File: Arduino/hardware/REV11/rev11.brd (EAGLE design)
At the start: 71 x 53 mm, 30 parts, among them IC2 ATMEGA168-AU, Q1 32768Hz

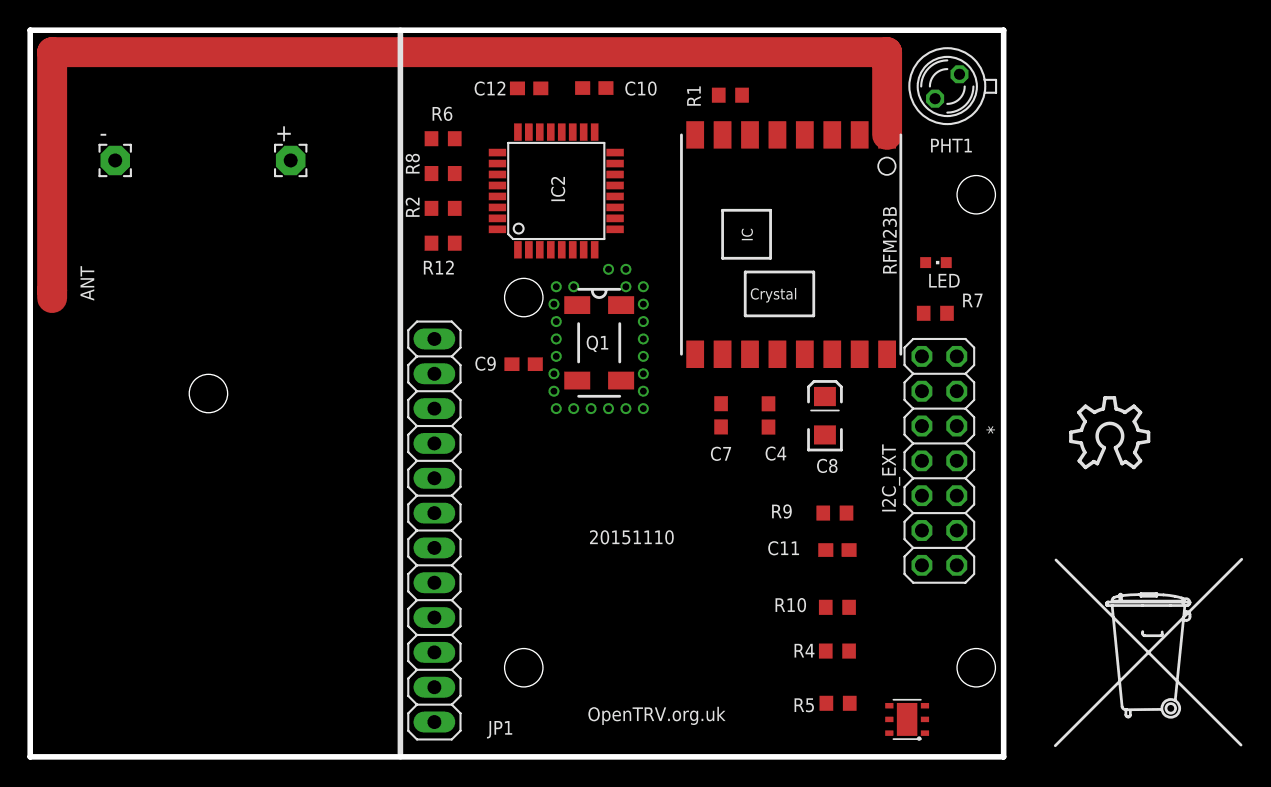
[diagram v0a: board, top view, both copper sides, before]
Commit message: boards routed once again
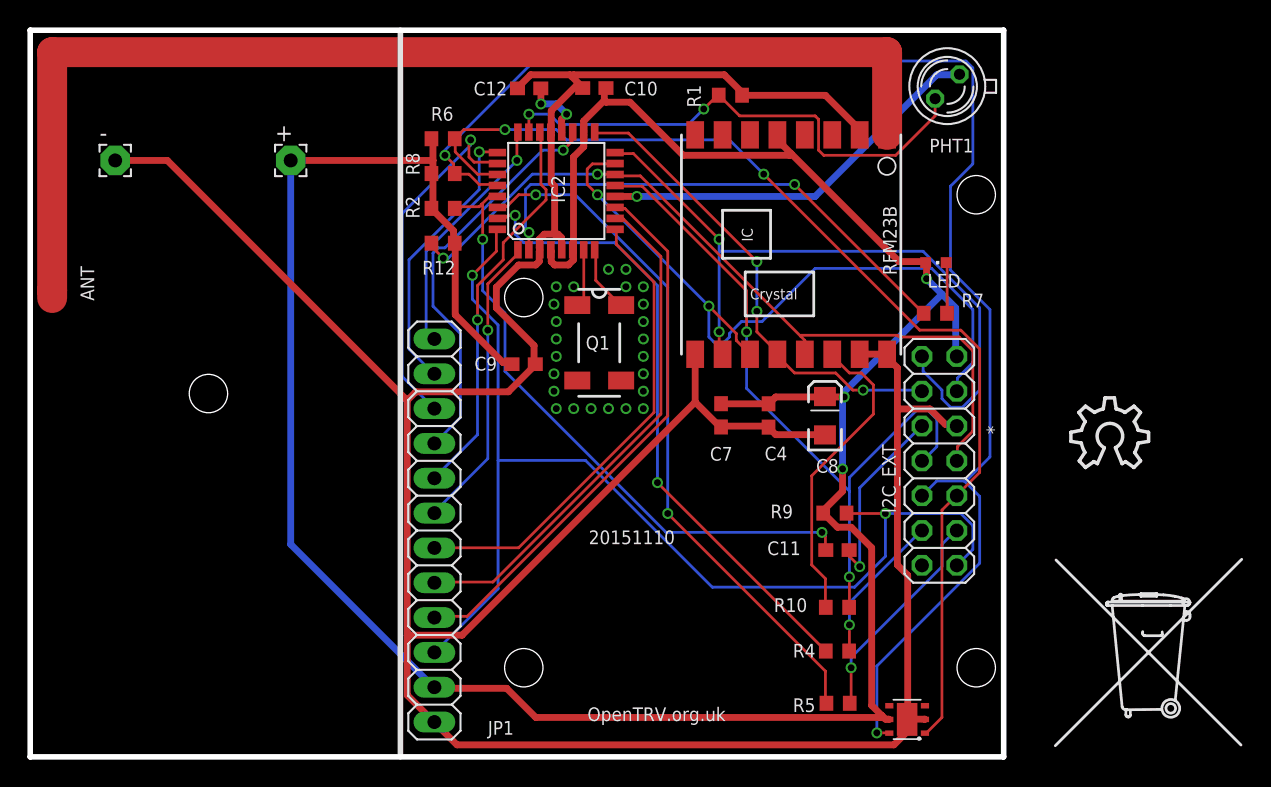
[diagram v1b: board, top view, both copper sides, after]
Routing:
- net GND: track 0.00 -> 233.4 mm
- net VCC: track 0.00 -> 207.1 mm, vias 0 -> 3
- net SCL: track 0.00 -> 106.1 mm, vias 0 -> 2
- net D2: track 0.00 -> 83.4 mm, vias 0 -> 2
- net SDA: track 0.00 -> 79.6 mm, vias 0 -> 2
- net SPI_NSS: track 0.00 -> 58.0 mm, vias 0 -> 2
- net SPI_MISO: track 0.00 -> 52.6 mm, vias 0 -> 2
- net SPI_MOSI: track 0.00 -> 52.3 mm, vias 0 -> 2
- net RFM_IRQ: track 0.00 -> 52.1 mm, vias 0 -> 2
- net TX: track 0.00 -> 50.7 mm, vias 0 -> 2
- net RX: track 0.00 -> 46.5 mm, vias 0 -> 2
- net RESET: track 0.00 -> 45.8 mm, vias 0 -> 2
- net D7: track 0.00 -> 40.3 mm
- net LDR: track 0.00 -> 37.7 mm, vias 0 -> 2
- net D6: track 0.00 -> 37.6 mm
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
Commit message: rev11 with ground plane
got bored enough to do this one :-D
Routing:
- net GND: track 233.4 -> 29.9 mm, vias 0 -> 39
- net RESET: track 45.8 -> 105.5 mm, vias 2 -> 0
- net SDA: track 79.6 -> 125.2 mm, vias 2 -> 0
- net VCC: track 207.1 -> 174.3 mm, vias 3 -> 0
- net TX: track 50.7 -> 74.2 mm, vias 2 -> 4
- net SPI_MISO: track 52.6 -> 42.5 mm, vias 2 -> 4
- net LDR: track 37.7 -> 47.1 mm
- net A6: track 29.7 -> 36.4 mm, vias 1 -> 2
- net SPI_MOSI: track 52.3 -> 46.1 mm, vias 2 -> 4
- net N$7: track 22.5 -> 26.9 mm, vias 0 -> 2
- net D7: track 40.3 -> 44.6 mm, vias 0 -> 2
- net RX: track 46.5 -> 50.2 mm
- net RFM_IRQ: track 52.1 -> 55.7 mm
- net SPI_NSS: track 58.0 -> 54.7 mm, vias 2 -> 5
- net A7: track 28.8 -> 31.5 mm
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- added copper zone on layer 1, net GND
- added copper zone on layer 16, net GND
